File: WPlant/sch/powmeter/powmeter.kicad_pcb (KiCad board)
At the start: 2 copper layers, 27.3 x 59.7 mm, 43 parts, among them J1 Input, J2 Out-L, J3 PROG/SWD, J4 Data, J5 Out-N, U1 BL0942, U2 PY32F003F18P6TU, U3 CA-IS3721CHS, U4 TLV70433DBVR

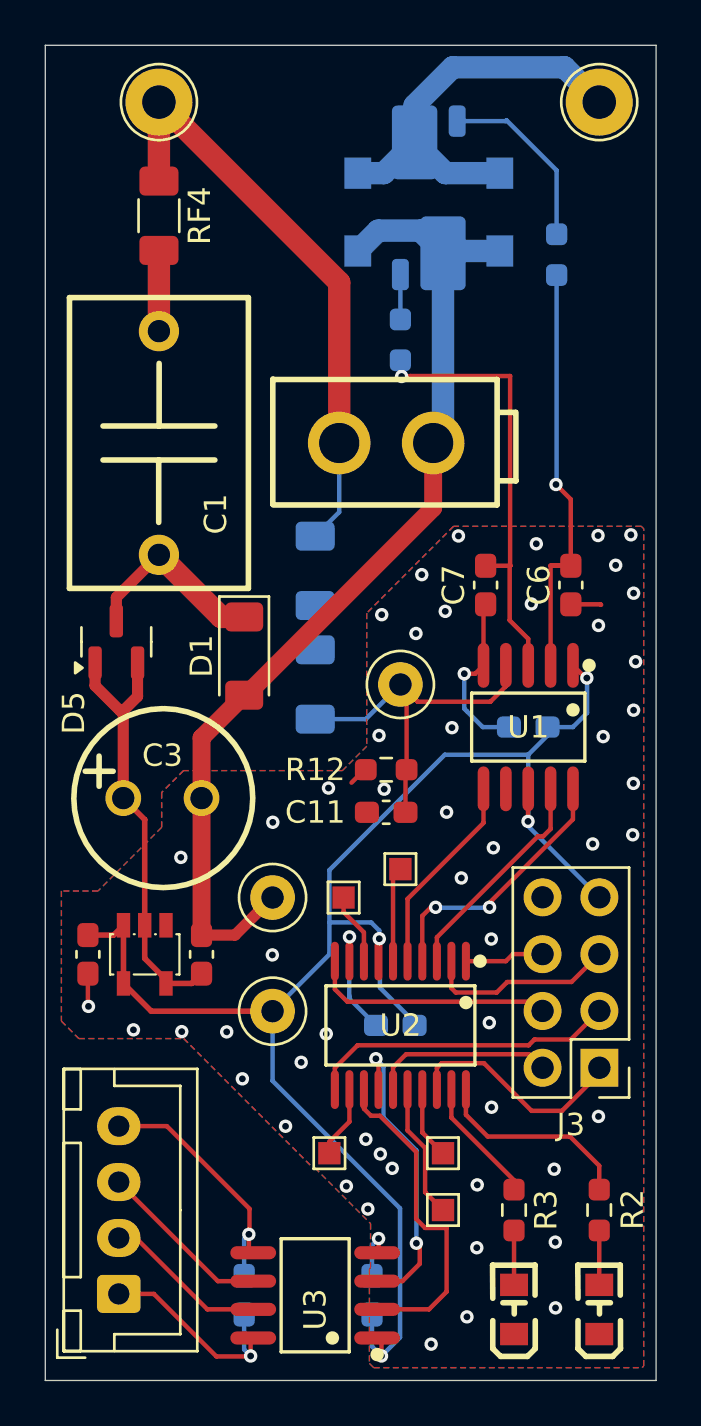
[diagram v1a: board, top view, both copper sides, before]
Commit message: Updated PCB for extension and powermeter
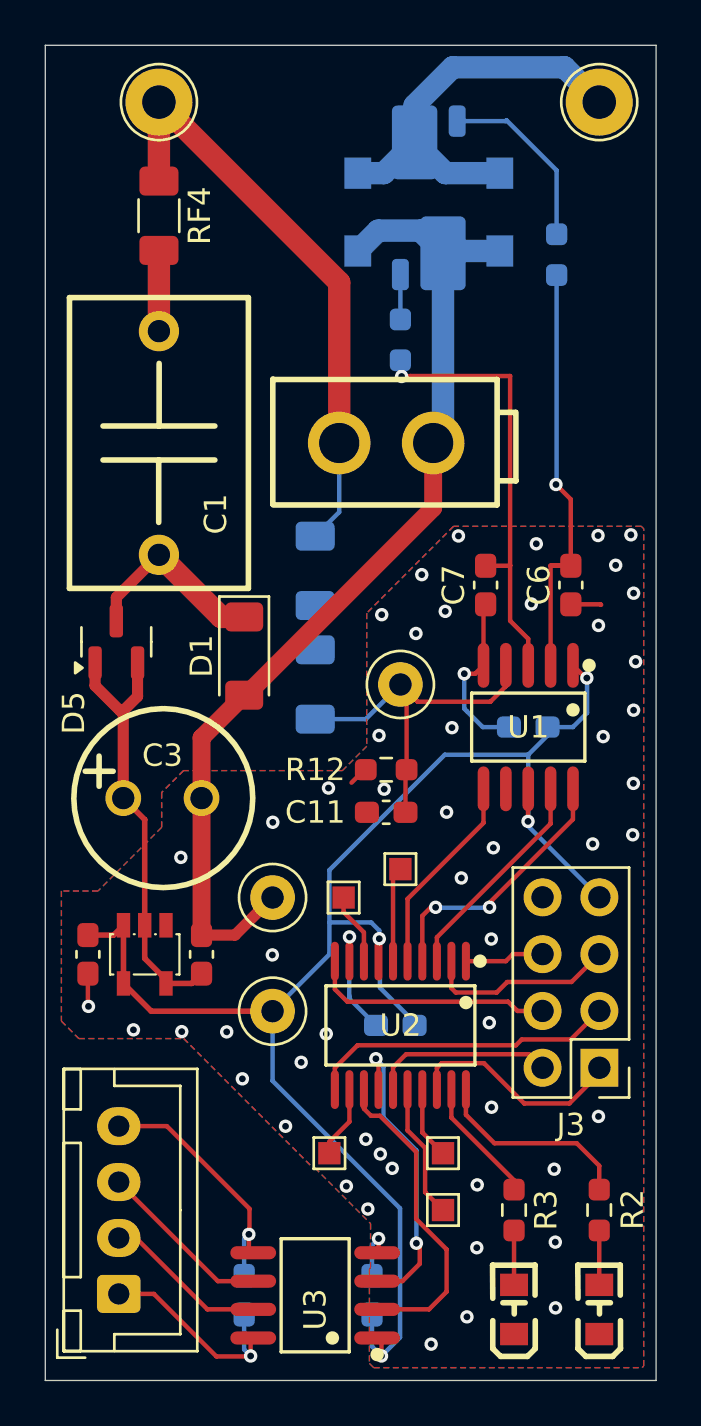
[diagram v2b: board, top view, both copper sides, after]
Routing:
- net Net-(U2-PB6): track 14.8 -> 14.2 mm
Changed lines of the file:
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@@
+	)
+	(segment
+		(start 171.25 78.92)
+		(end 175.72 78.92)
+		(width 0.2)
+		(layer "F.Cu")
+		(net 8)
+	)
+	(segment
+		(start 175.72 87.3925)
+		(end 175.72 89.86)
+		(width 0.2)
+		(layer "F.Cu")
+		(net 8)
+	)
+	(segment
+		(start 171.23 78.94)
+		(end 171.25 78.92)
+		(width 0.2)
+		(layer "F.Cu")
+		(net 8)
+	)
+	(segment
+		(start 175.71 87.4025)
+		(end 175.72 87.3925)
+		(width 0.2)
+		(layer "F.Cu")
+		(net 8)
+	)
+	(segment
+		(start 174.625 87.4025)
+		(end 175.71 87.4025)
+		(width 0.2)
+		(layer "F.Cu")
+		(net 8)
 	)
 	(segment
@@
 	)
 	(segment
-		(start 175.7 87.4325)
-		(end 175.7 89.84)
-		(width 0.2)
-		(layer "F.Cu")
-		(net 8)
-	)
-	(segment
-		(start 171.23 78.94)
-		(end 171.25 78.92)
+		(start 175.72 89.86)
+		(end 176.53 90.67)
 		(width 0.2)
 		(layer "F.Cu")
@@
 	)
 	(segment
-		(start 175.7 89.84)
-		(end 176.53 90.67)
-		(width 0.2)
-		(layer "F.Cu")
-		(net 8)
-	)
-	(segment
 		(start 176.53 90.67)
 		(end 176.53 91.855)
-		(width 0.2)
-		(layer "F.Cu")
-		(net 8)
-	)
-	(segment
-		(start 175.72 87.3925)
-		(end 175.73 87.4025)
-		(width 0.2)
-		(layer "F.Cu")
-		(net 8)
-	)
-	(segment
-		(start 174.625 87.4025)
-		(end 175.73 87.4025)
-		(width 0.2)
-		(layer "F.Cu")
-		(net 8)
-	)
-	(segment
-		(start 175.73 87.4025)
-		(end 175.7 87.4325)
-		(width 0.2)
-		(layer "F.Cu")
-		(net 8)
-	)
-	(segment
-		(start 171.25 78.92)
-		(end 175.72 78.92)
 		(width 0.2)
 		(layer "F.Cu")
@@
 	)
 	(segment
-		(start 178.4 112.92)
+		(start 173.745 111.945)
+		(end 175.02 113.22)
+		(width 0.2)
+		(layer "F.Cu")
+		(net 15)
+	)
+	(segment
+		(start 178.7 113.22)
 		(end 179.705 114.225)
 		(width 0.2)
@@
 	)
 	(segment
-		(start 174.72 112.92)
-		(end 178.4 112.92)
-		(width 0.2)
-		(layer "F.Cu")
-		(net 15)
-	)
-	(segment
-		(start 173.745 111.945)
-		(end 174.72 112.92)
+		(start 173.745 110.82)
+		(end 173.745 111.945)
 		(width 0.2)
 		(layer "F.Cu")
@@
 	)
 	(segment
-		(start 173.745 110.82)
-		(end 173.745 111.945)
+		(start 175.02 113.22)
+		(end 178.7 113.22)
 		(width 0.2)
 		(layer "F.Cu")
@@
 	(segment
 		(start 177.53 97.375)
-		(end 177.53 99.17)
-		(width 0.2)
-		(layer "F.Cu")
-		(net 22)
-	)
-	(segment
-		(start 176.96 99.5)
-		(end 172.445 104.015)
+		(end 177.53 98.93)
 		(width 0.2)
 		(layer "F.Cu")
@@
 	)
 	(segment
-		(start 177.53 99.17)
-		(end 177.2 99.5)
-		(width 0.2)
-		(layer "F.Cu")
-		(net 22)
-	)
-	(segment
-		(start 177.2 99.5)
-		(end 176.96 99.5)
+		(start 177.53 98.93)
+		(end 172.445 104.015)
 		(width 0.2)
 		(layer "F.Cu")
@@
 	)
 	(segment
+		(start 169.775 120.645)
+		(end 172.095 120.645)
+		(width 0.2)
+		(layer "F.Cu")
+		(net 25)
+	)
+	(segment
 		(start 172.095 120.645)
 		(end 172.88 119.86)
@@
 	)
 	(segment
+		(start 169.185 111.675)
+		(end 169.185 110.82)
+		(width 0.2)
+		(layer "F.Cu")
+		(net 25)
+	)
+	(segment
+		(start 172.88 117.965)
+		(end 171.52 116.605)
+		(width 0.2)
+		(layer "F.Cu")
+		(net 25)
+	)
+	(segment
+		(start 169.5 111.99)
+		(end 169.185 111.675)
+		(width 0.2)
+		(layer "F.Cu")
+		(net 25)
+	)
+	(segment
 		(start 169.9 111.99)
 		(end 169.5 111.99)
@@
 	)
 	(segment
-		(start 169.5 111.99)
-		(end 169.185 111.675)
-		(width 0.2)
-		(layer "F.Cu")
-		(net 25)
-	)
-	(segment
-		(start 172.88 117.005)
-		(end 171.92 117.005)
-		(width 0.2)
-		(layer "F.Cu")
-		(net 25)
-	)
-	(segment
-		(start 169.185 111.675)
-		(end 169.185 110.82)
-		(width 0.2)
-		(layer "F.Cu")
-		(net 25)
-	)
-	(segment
 		(start 171.52 116.605)
 		(end 171.52 113.61)
@@
 	(segment
 		(start 172.88 119.86)
-		(end 172.88 117.005)
-		(width 0.2)
-		(layer "F.Cu")
-		(net 25)
-	)
-	(segment
-		(start 171.92 117.005)
-		(end 171.52 116.605)
-		(width 0.2)
-		(layer "F.Cu")
-		(net 25)
-	)
-	(segment
-		(start 169.775 120.645)
-		(end 172.095 120.645)
+		(end 172.88 117.965)
 		(width 0.2)
 		(layer "F.Cu")
@@
 	)
 	(segment
-		(start 176.755 106.89)
-		(end 168.44 106.89)
+		(start 176.045 107.305)
+		(end 175.63 106.89)
 		(width 0.2)
 		(layer "F.Cu")
@@
 	)
 	(segment
+		(start 177.17 107.305)
+		(end 176.045 107.305)
+		(width 0.2)
+		(layer "F.Cu")
+		(net 32)
+	)
+	(segment
 		(start 167.885 106.335)
 		(end 167.885 105.08)
@@
 	)
 	(segment
-		(start 177.17 107.305)
-		(end 176.755 106.89)
+		(start 175.63 106.89)
+		(end 168.44 106.89)
 		(width 0.2)
 		(layer "F.Cu")
@@
 	)
 	(segment
+		(start 172.445 109.855)
+		(end 172.445 110.82)
+		(width 0.2)
+		(layer "F.Cu")
+		(net 36)
+	)
+	(segment
+		(start 179.71 109.845)
+		(end 179.71 110.1)
+		(width 0.2)
+		(layer "F.Cu")
+		(net 36)
+	)
+	(segment
+		(start 174.55 109.64)
+		(end 172.66 109.64)
+		(width 0.2)
+		(layer "F.Cu")
+		(net 36)
+	)
+	(segment
+		(start 179.71 110.1)
+		(end 178.37 111.44)
+		(width 0.2)
+		(layer "F.Cu")
+		(net 36)
+	)
+	(segment
 		(start 172.66 109.64)
 		(end 172.445 109.855)
@@
 	)
 	(segment
-		(start 179.71 109.845)
-		(end 179.71 110.1)
+		(start 176.35 111.44)
+		(end 174.55 109.64)
 		(width 0.2)
 		(layer "F.Cu")
@@
 	)
 	(segment
-		(start 176.68 111.77)
-		(end 174.55 109.64)
+		(start 178.37 111.44)
+		(end 176.35 111.44)
 		(width 0.2)
 		(layer "F.Cu")
@@
 	)
 	(segment
-		(start 172.445 109.855)
-		(end 172.445 110.82)
-		(width 0.2)
-		(layer "F.Cu")
-		(net 36)
-	)
-	(segment
-		(start 178.04 111.77)
-		(end 176.68 111.77)
-		(width 0.2)
-		(layer "F.Cu")
-		(net 36)
-	)
-	(segment
-		(start 174.55 109.64)
-		(end 172.66 109.64)
-		(width 0.2)
-		(layer "F.Cu")
-		(net 36)
-	)
-	(segment
-		(start 179.71 110.1)
-		(end 178.04 111.77)
-		(width 0.2)
-		(layer "F.Cu")
-		(net 36)
-	)
-	(segment
-		(start 176.808654 108.58)
-		(end 176.548654 108.84)
+		(start 178.435 108.58)
+		(end 176.24 108.58)
 		(width 0.2)
 		(layer "F.Cu")
@@
 	)
 	(segment
-		(start 178.435 108.58)
-		(end 176.808654 108.58)
+		(start 167.885 109.855)
+		(end 167.885 110.82)
+		(width 0.2)
+		(layer "F.Cu")
+		(net 37)
+	)
+	(segment
+		(start 168.9 108.84)
+		(end 167.885 109.855)
+		(width 0.2)
+		(layer "F.Cu")
+		(net 37)
+	)
+	(segment
+		(start 176.24 108.58)
+		(end 175.98 108.84)
 		(width 0.2)
 		(layer "F.Cu")
@@
 	)
 	(segment
-		(start 176.548654 108.84)
+		(start 175.98 108.84)
 		(end 168.9 108.84)
 		(width 0.2)
 		(layer "F.Cu")
-		(net 37)
-	)
-	(segment
-		(start 168.9 108.84)
-		(end 167.885 109.855)
-		(width 0.2)
-		(layer "F.Cu")
-		(net 37)
-	)
-	(segment
-		(start 167.885 109.855)
-		(end 167.885 110.82)
-		(width 0.2)
-		(layer "F.Cu")
